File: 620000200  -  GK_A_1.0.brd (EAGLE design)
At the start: 91.4 x 53.3 mm, 64 parts, among them IC1 PIC18F26K22, IC6 REG1117, Q1 16MHz, Q2 12MHz, T1 BCR505-W, T2 BCR505-W, U1 74AHC1G08DBV, U3 74AHC1G32DBV

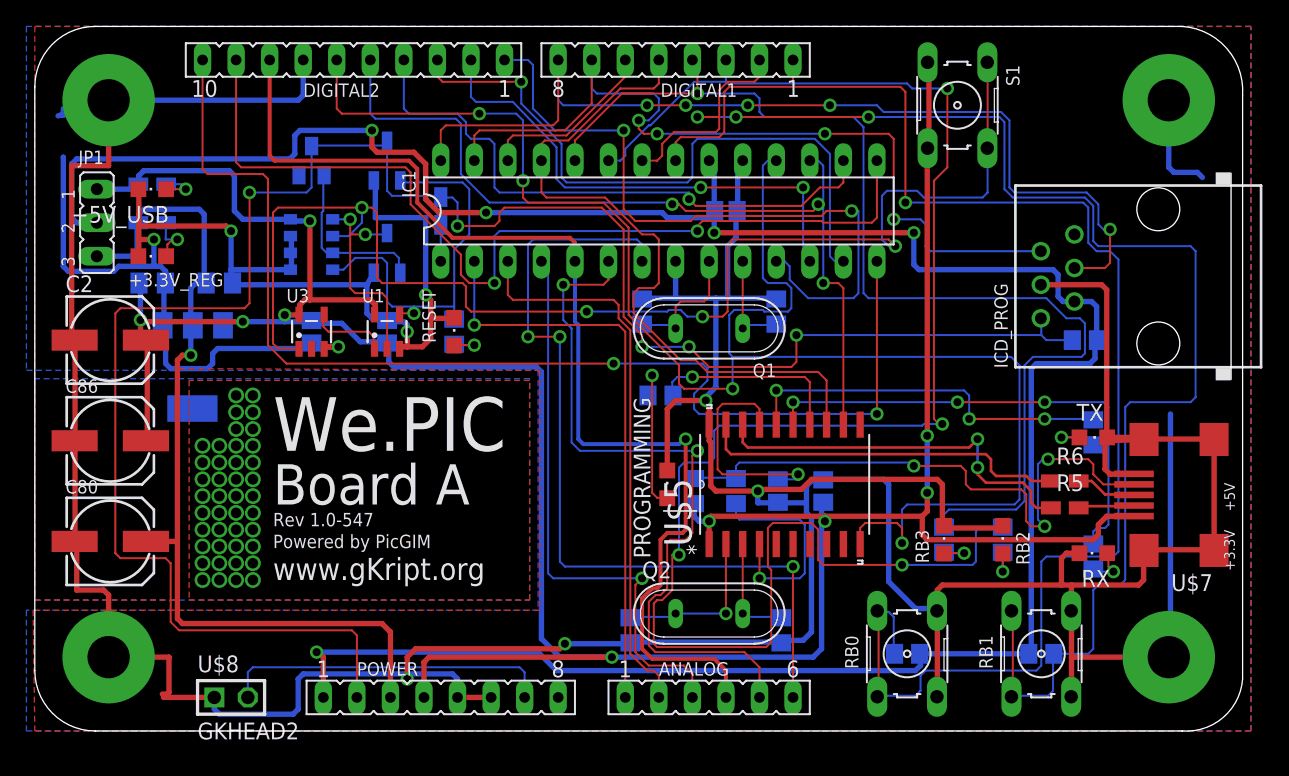
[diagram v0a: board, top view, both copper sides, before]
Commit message: Progetto pronto per rifare con le nuove MCU. Mantenuto : Alimentazione Reset Struttura arduino compatibile
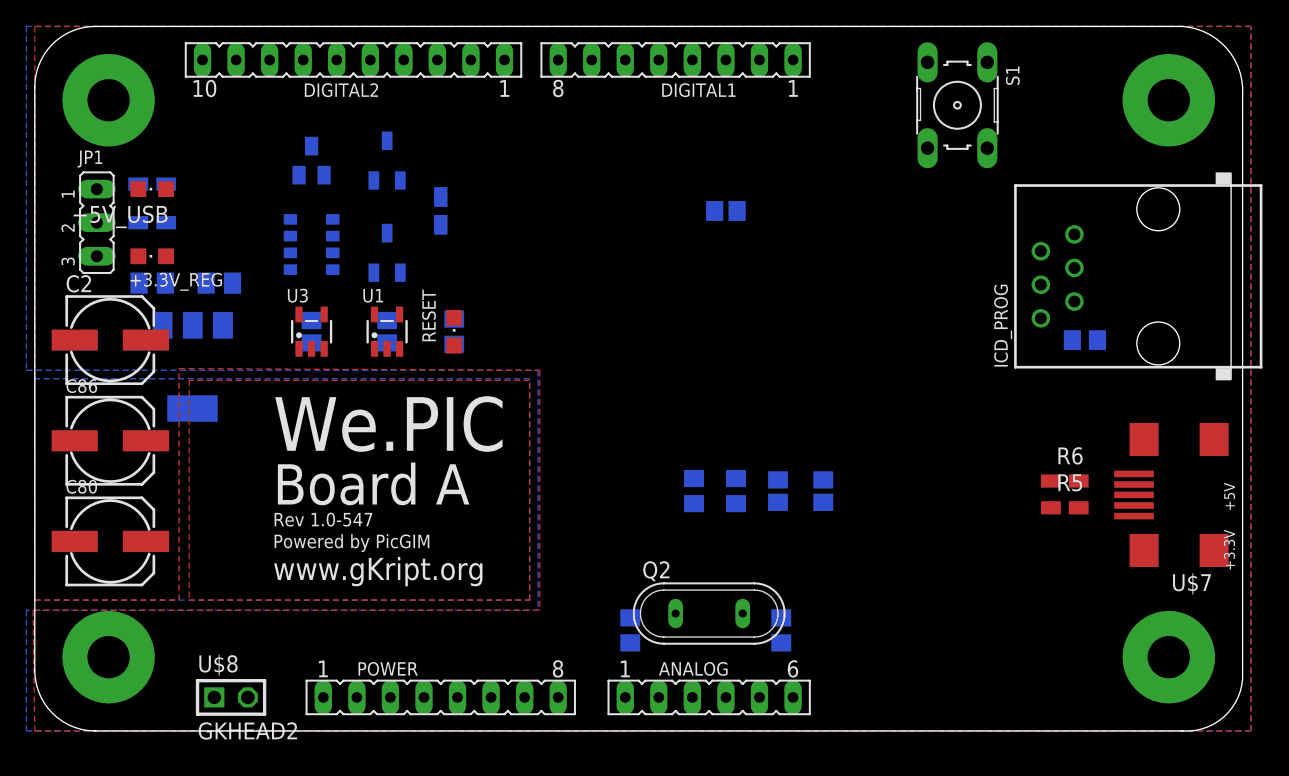
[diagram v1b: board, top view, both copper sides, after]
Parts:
- removed C3, C7: 22p, rcl:C0805
- removed IC1: PIC18F26K22, microchip:DIL28-3
- removed PROGRAMMING, RB2, RB3, RX, TX: (no value), led:CHIPLED_0805
- removed Q1: 16MHz, special:QS
- removed R11, R12: 10K, rcl:R0805
- removed R13, R2, R21, R3, R4: 1K, rcl:R0805
- removed RB0, RB1: (no value), switch-omron:B3F-10XX
- removed U$5: PIC18LF14K50-I/SO, gkripthw:SOIC127P1030X265-20N
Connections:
- removed net N$1: IC1.1, R30.2
- removed net N$15: R2.2, U$5.16
- removed net N$16: R3.2, U$5.15
- removed net N$17: R2.1, TX.A
- removed net N$18: R3.1, RX.A
- removed net N$21: C3.2, IC1.9, Q1.2
- removed net N$22: C7.2, IC1.10, Q1.1
- removed net N$24: PROGRAMMING.A, R4.1
- removed net N$25: R4.2, U$5.14
- removed net N$28: R8.2, U$5.4
- removed net N$3: R21.2, RB3.A
- removed net N$5: R13.2, RB2.A
- removed net PORTA0: ANALOG.1, IC1.2
- removed net PORTA1: ANALOG.2, IC1.3
- removed net PORTA2: ANALOG.3, IC1.4
- removed net PORTA3: ANALOG.4, DIGITAL2.8, IC1.5
- removed net PORTA4: ANALOG.5, IC1.6
- removed net PORTA5: ANALOG.6, IC1.7
- removed net PORTB0: DIGITAL1.1, IC1.21, R12.1, RB0.1, RB0.2
- removed net PORTB1: DIGITAL1.2, IC1.22, R11.1, RB1.1, RB1.2
- removed net PORTB2: DIGITAL1.3, IC1.23, R13.1
- removed net PORTB3: DIGITAL1.4, IC1.24, R21.1
- removed net PORTB4: DIGITAL1.5, IC1.25, U$5.13
- removed net PORTB5: DIGITAL1.6, IC1.26
- removed net PORTC0: DIGITAL2.1, IC1.11
- removed net PORTC1: DIGITAL2.2, IC1.12
- removed net PORTC2: DIGITAL2.3, IC1.13
- removed net PORTC3: DIGITAL2.10, IC1.14
- removed net PORTC4: DIGITAL2.9, IC1.15
- removed net PORTC5: DIGITAL2.4, IC1.16
- removed net PORTC6: DIGITAL2.5, IC1.17, U$5.12
- removed net PORTC7: DIGITAL2.6, IC1.18, U$5.10
- net +5V: no longer U$5.1
- net GND: no longer C3.1, C7.1, DIGITAL2.7, IC1.19, IC1.8, PROGRAMMING.C, RB0.3, RB0.4, RB1.3, RB1.4, RB2.C, RB3.C, RX.C, TX.C, U$5.20
- net N$10: no longer U$5.19
- net N$13: no longer U$5.2
- net N$26: no longer U$5.17
- net N$8: no longer U$5.3
- net N$9: no longer U$5.18
- net PORTB6: no longer DIGITAL1.7, IC1.27
- net PORTB7: no longer DIGITAL1.8, IC1.28
- net VCC: no longer IC1.20, R11.2, R12.2
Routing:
- net GND: track 477.3 -> 0.00 mm, vias 9 -> 0
- net +5V: track 228.2 -> 0.00 mm, vias 9 -> 0
- net VCC: track 192.0 -> 0.00 mm, vias 5 -> 0
- net _MCLR: track 150.9 -> 0.00 mm, vias 5 -> 0
- net PORTB2: track 134.7 -> 0.00 mm, vias 4 -> 0
- net PORTC7: track 124.7 -> 0.00 mm, vias 4 -> 0
- net PORTB1: track 116.0 -> 0.00 mm, vias 3 -> 0
- net PORTB0: track 113.5 -> 0.00 mm, vias 1 -> 0
- net PUSH_RESET: track 99.7 -> 0.00 mm, vias 4 -> 0
- net PORTC3: track 89.1 -> 0.00 mm, vias 2 -> 0
- net PORTA3: track 85.4 -> 0.00 mm, vias 1 -> 0
- net PORTB3: track 84.5 -> 0.00 mm, vias 1 -> 0
- net PORTB7: track 74.2 -> 0.00 mm, vias 5 -> 0
- net PORTC4: track 71.1 -> 0.00 mm, vias 2 -> 0
- net +3V3: track 68.2 -> 0.00 mm, vias 1 -> 0
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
